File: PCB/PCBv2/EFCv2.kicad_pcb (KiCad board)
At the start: 2 copper layers, 64.8 x 64.8 mm, 58 parts, among them J1 USB_B_Micro, J2 Conn_02x03_Odd_Even, M1 Motor_DC, Q1 Q_Photo_NPN, SW1 SW_Push, SW2 SW_Push, SW3 SW_Push, SW4 SW_Push, U1 MCP4725, U2 LM386, U3 SST25VF020B, U4 ATmega328PB-AU, U5 MCP7940N, U6 DRV2605L, Y1 Resonator, Y2 Crystal_Small

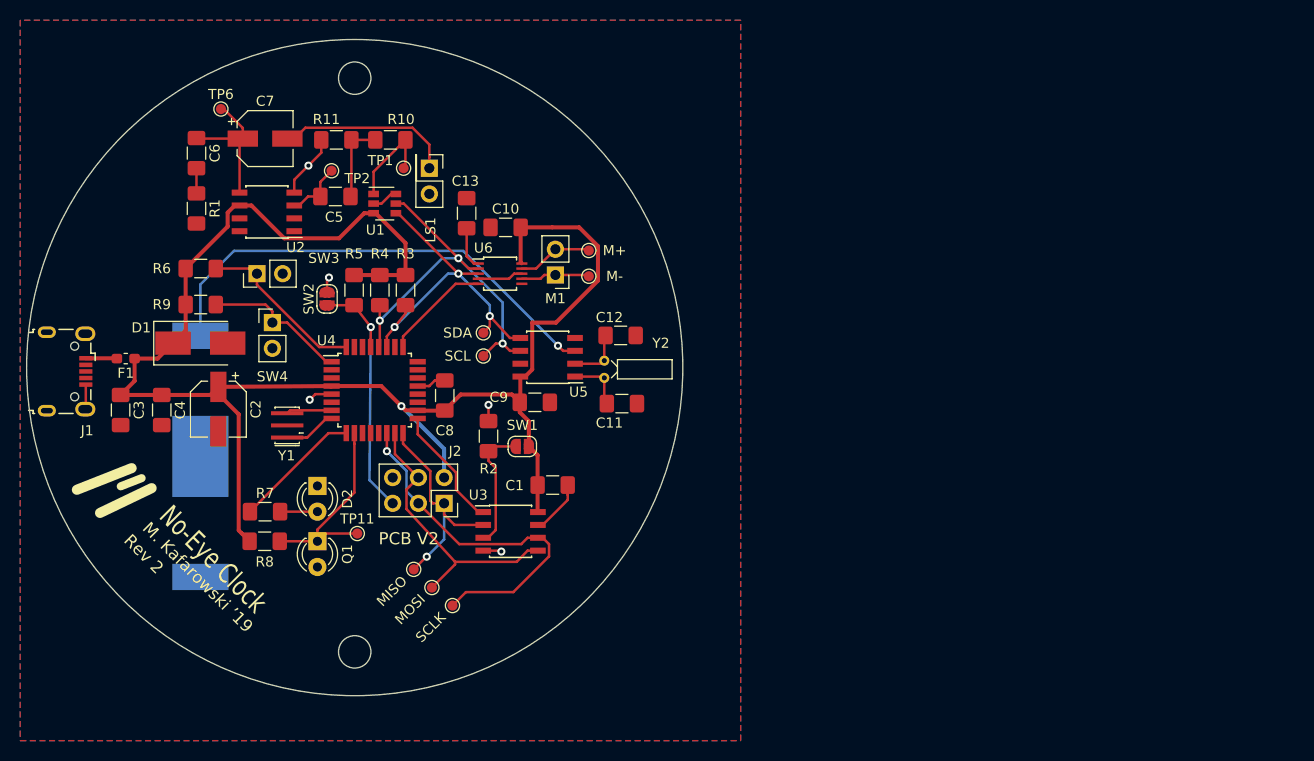
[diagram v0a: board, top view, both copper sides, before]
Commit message: Fixed multiple issues with previous board surrounding audio and memory system
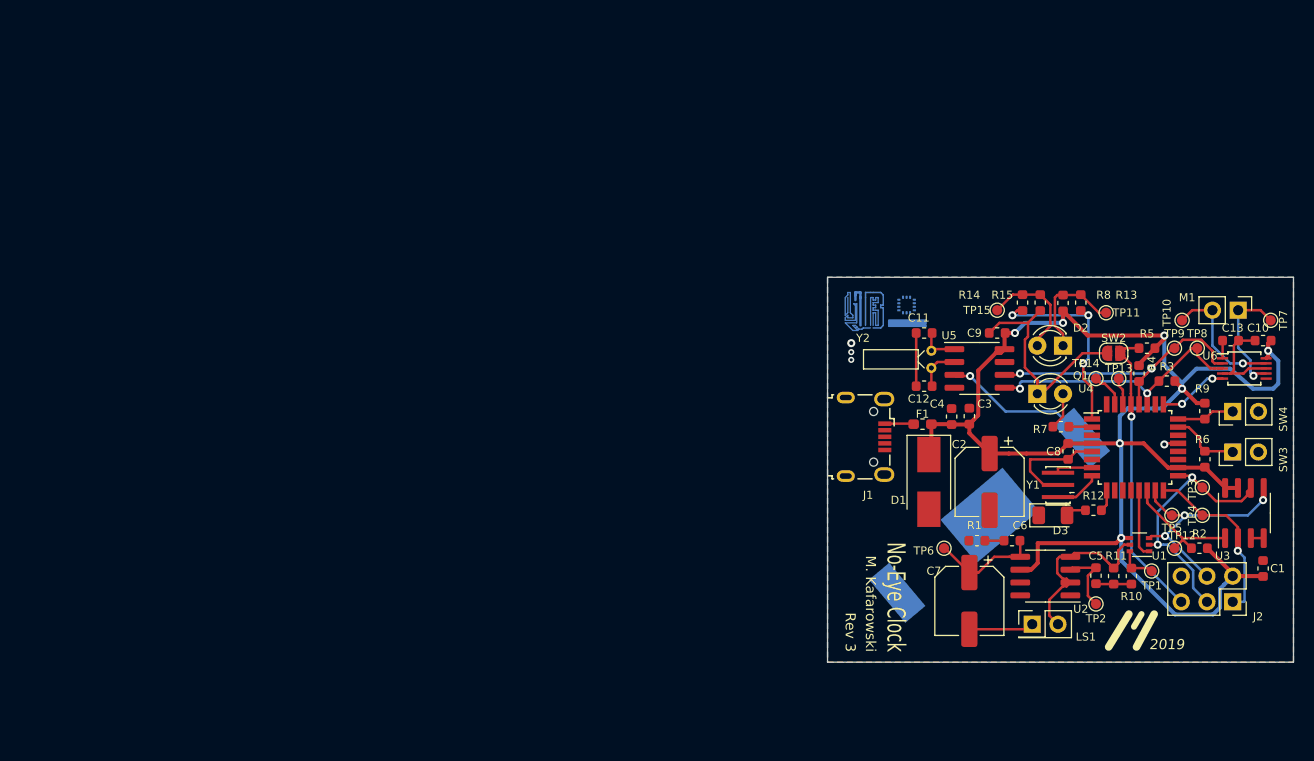
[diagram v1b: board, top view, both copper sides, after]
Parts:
- removed ? (x2): MountingHole_3.2mm_M3, MountingHole:MountingHole_3.2mm_M3
- removed M+, M-, MISO, MOSI, SCL, SCLK, SDA: TestPoint, TestPoint:TestPoint_Pad_D1.0mm
- removed SW1: SW_Push, Jumper:SolderJumper-2_P1.3mm_Open_RoundedPad1.0x1.5mm
- added D3: IR204A, LED_SMD:LED_1206_3216Metric, F.Cu at (152.8, 96.5)
- added R12: 10K, Resistor_SMD:R_0603_1608Metric, F.Cu at (156.8, 96.0)
- added R13: 0R, Resistor_SMD:R_0603_1608Metric, F.Cu at (155.5, 75.5)
- added R14: 0R, Resistor_SMD:R_0603_1608Metric, F.Cu at (149.8, 75.5)
- added R15: R, Resistor_SMD:R_0603_1608Metric, F.Cu at (151.5, 75.5)
- added REF**: LGA-14_2x2mm_P0.35mm_LayoutBorder3x4y, Package_LGA:LGA-14_2x2mm_P0.35mm_LayoutBorder3x4y, B.Cu at (138.3, 75.7)
- added TP10: TestPoint, TestPoint:TestPoint_Pad_D1.0mm, F.Cu at (165.5, 77.2)
- added TP12: TestPoint, TestPoint:TestPoint_Pad_D1.0mm, F.Cu at (164.8, 99.8)
- added TP13: TestPoint, TestPoint:TestPoint_Pad_D1.0mm, F.Cu at (159.2, 83.0)
- added TP14: TestPoint, TestPoint:TestPoint_Pad_D1.0mm, F.Cu at (157.0, 83.0)
- added TP15: TestPoint, TestPoint:TestPoint_Pad_D1.0mm, F.Cu at (147.2, 76.2)
- added TP3: TestPoint, TestPoint:TestPoint_Pad_D1.0mm, F.Cu at (167.5, 93.8)
- added TP4: TestPoint, TestPoint:TestPoint_Pad_D1.0mm, F.Cu at (167.5, 96.5)
- added TP5: TestPoint, TestPoint:TestPoint_Pad_D1.0mm, F.Cu at (164.5, 96.5)
- added TP7: TestPoint, TestPoint:TestPoint_Pad_D1.0mm, F.Cu at (174.2, 77.2)
- added TP8: TestPoint, TestPoint:TestPoint_Pad_D1.0mm, F.Cu at (167.0, 80.0)
- added TP9: TestPoint, TestPoint:TestPoint_Pad_D1.0mm, F.Cu at (164.8, 80.0)
- C1, C11, C12, C3, C4, C5, C6, C8, C9: footprint Capacitor_SMD:C_1206_3216Metric_Pad1.42x1.75mm_HandSolder -> Capacitor_SMD:C_0603_1608Metric
- C10, C13: value 0.1uF -> 1uF; footprint Capacitor_SMD:C_1206_3216Metric_Pad1.42x1.75mm_HandSolder -> Capacitor_SMD:C_0603_1608Metric
- C2, C7: footprint Capacitor_SMD:CP_Elec_5x3 -> Capacitor_SMD:CP_Elec_6.3x5.9
- R1, R10, R11, R2, R3, R4, R5, R6, R7, R9: footprint Resistor_SMD:R_1206_3216Metric_Pad1.42x1.75mm_HandSolder -> Resistor_SMD:R_0603_1608Metric
- R8: value 10K -> R; footprint Resistor_SMD:R_1206_3216Metric_Pad1.42x1.75mm_HandSolder -> Resistor_SMD:R_0603_1608Metric
- U1: value MCP4725 -> LTC2630; footprint Package_TO_SOT_SMD:SOT-23-6 -> Package_TO_SOT_SMD:SOT-363_SC-70-6
- U3: value SST25VF020B -> AT25M01
- moved R6 100.9 mm to (167.8, 91.0), turned to 90 degrees
- moved R9 99.7 mm to (167.8, 86.2), turned to 270 degrees
- moved SW3 97.9 mm to (170.5, 90.2)
- moved SW4 95.2 mm to (170.5, 86.2), turned to 90 degrees
- moved C6 89.1 mm to (148.7, 99.0), turned to 180 degrees
- moved R11 88.0 mm to (158.8, 102.5), turned to 90 degrees
- moved TP2 86.7 mm to (157.0, 105.2), turned to 180 degrees
- moved R10 84.9 mm to (160.5, 102.5), turned to 270 degrees
- moved U2 84.8 mm to (152.0, 102.5)
- moved C5 83.9 mm to (157.0, 102.5), turned to 270 degrees
- moved TP1 83.9 mm to (162.5, 102.0), turned to 180 degrees
- moved C3 83.8 mm to (144.5, 86.7), turned to 90 degrees
- moved R1 83.7 mm to (145.2, 99.0), turned to 180 degrees
- moved TP6 83.5 mm to (142.0, 99.8), turned to 180 degrees
- moved C7 83.2 mm to (144.5, 105.0), turned to 270 degrees
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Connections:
- net Net-(U4-Pad7) renamed /XTAL1
- net Net-(U4-Pad8) renamed /XTAL2
- Q1 pad 1: /IR_DETECT -> Net-(Q1-Pad1)
- Q1 pad 2: GND -> Net-(Q1-Pad2)
- R2 pad 1: Net-(R2-Pad1) -> /EEPROM_EN
- R2 pad 2: GND -> +5V
- R8 pad 2: /IR_DETECT -> Net-(Q1-Pad1)
- TP11 pad 1: /IR_DETECT -> Net-(Q1-Pad1)
- U1 pad 1: Net-(R10-Pad1) -> /DAC_EN
- U1 pad 2: GND -> /SCLK
- U1 pad 3: +5V -> /MOSI
- U1 pad 4: /SDA -> +5V
- U1 pad 5: /SCL -> GND
- U1 pad 6: GND -> Net-(R10-Pad1)
- U3 pad 1: /FLASH_EN -> /EEPROM_EN
- U3 pad 3: Net-(R2-Pad1) -> GND
- U3 pad 7: GND -> +5V
- U4 pad 1: /BUTTON_SET -> /IR_DETECT
- U4 pad 10: /IR_DETECT -> Net-(U4-Pad10)
- U4 pad 13: Net-(U4-Pad13) -> /DAC_EN
- U4 pad 14: /SCLK -> /EEPROM_EN
- U4 pad 17: /FLASH_EN -> /SCLK
- U4 pad 2: Net-(U4-Pad2) -> /IR_LED
- U4 pad 23: Net-(U4-Pad23) -> /BUTTON_MODE
- U4 pad 24: Net-(U4-Pad24) -> /BUTTON_SET
- U4 pad 30: Net-(U4-Pad30) -> /RX
- U4 pad 31: Net-(U4-Pad31) -> /TX
- U4 pad 32: /BUTTON_MODE -> Net-(U4-Pad32)
- U4 pad 9: /IR_LED -> /LED
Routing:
- net GND: track 31.5 -> 114.9 mm, vias 5 -> 4
- net Net-(BT1-Pad1): track 47.5 -> 15.2 mm
- net (no net): track 0.00 -> 21.0 mm
- net Net-(R2-Pad1): track 13.0 -> 0.00 mm
- net /EEPROM_EN: track 0.00 -> 12.9 mm
- net /FLASH_EN: track 12.2 -> 0.00 mm
- net /SCL: track 40.0 -> 28.6 mm, vias 3 -> 2
- net Net-(C7-Pad2): track 17.5 -> 6.42 mm
- net Net-(Q1-Pad1): track 0.00 -> 11.0 mm
- net Net-(Q1-Pad2): track 0.00 -> 10.7 mm
- net /SCLK: track 36.5 -> 26.1 mm, vias 1 -> 2
- net /IR_LED: track 12.7 -> 2.30 mm
- net +5V: track 164.9 -> 154.5 mm, vias 1 -> 7
- net /BUTTON_MODE: track 16.7 -> 6.87 mm
- net /BUTTON_SET: track 14.4 -> 5.71 mm
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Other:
- board size 64.8 x 64.8 mm -> 46 x 38 mm
- rule trace_min: 0.2 -> 0.0762
- board text added: "0.75 abcdefghijklmnopqrstuvwxyzABCDEFGHIJKLMNOPQRSTUVWXYZ0123456789"
- board text added: "2019"
- board text added: "M. Kafarowski"
- board text added: "Rev 3"
- board text removed: "M. Kafarowski ’19"
- board text removed: "PCB V2"
- board text removed: "Rev 2"
